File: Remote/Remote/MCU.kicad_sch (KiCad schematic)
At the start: 21 parts, among them J3 61300511121, J4 M20-9990246, U3 STM32G030F6Px, U4 NRF24L01_Breakout

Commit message: Added footprints
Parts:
- C5: footprint (none) -> Power_:CAPC1608X90N
- C6: footprint (none) -> MCU_:CAPC1005X55N
- R4: footprint (none) -> MCU_:RESC2012X65N
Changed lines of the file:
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@@
       (effects (font (size 1.27 1.27)))
     )
-    (property "Footprint" "" (at 148.59 120.9548 0)
+    (property "Footprint" "Power_:CAPC1608X90N" (at 148.59 120.9548 0)
       (effects (font (size 1.27 1.27)) hide)
     )
@@
       (effects (font (size 1.27 1.27)))
     )
-    (property "Footprint" "" (at 148.59 126.0348 0)
-      (effects (font (size 1.27 1.27)) hide)
-    )
-    (property "Datasheet" "~" (at 144.78 127 0)
+    (property "Footprint" "MCU_:CAPC1005X55N" (at 148.59 126.0348 0)
+      (effects (font (size 1.27 1.27)) hide)
+    )
+    (property "Datasheet" "CL05A104KA5NNNC" (at 144.78 127 0)
       (effects (font (size 1.27 1.27)) hide)
     )
@@
       (effects (font (size 1.27 1.27)))
     )
-    (property "Footprint" "" (at 207.01 103.378 90)
-      (effects (font (size 1.27 1.27)) hide)
-    )
-    (property "Datasheet" "~" (at 207.01 101.6 0)
-      (effects (font (size 1.27 1.27)) hide)
-    )
+    (property "Footprint" "MCU_:RESC2012X65N" (at 207.01 103.378 90)
+      (effects (font (size 1.27 1.27)) hide)
+    )
+    (property "Datasheet" "ESR10EZPF1200" (at 207.01 101.6 0)
+      (effects (font (size 1.27 1.27)) hide)
+    )

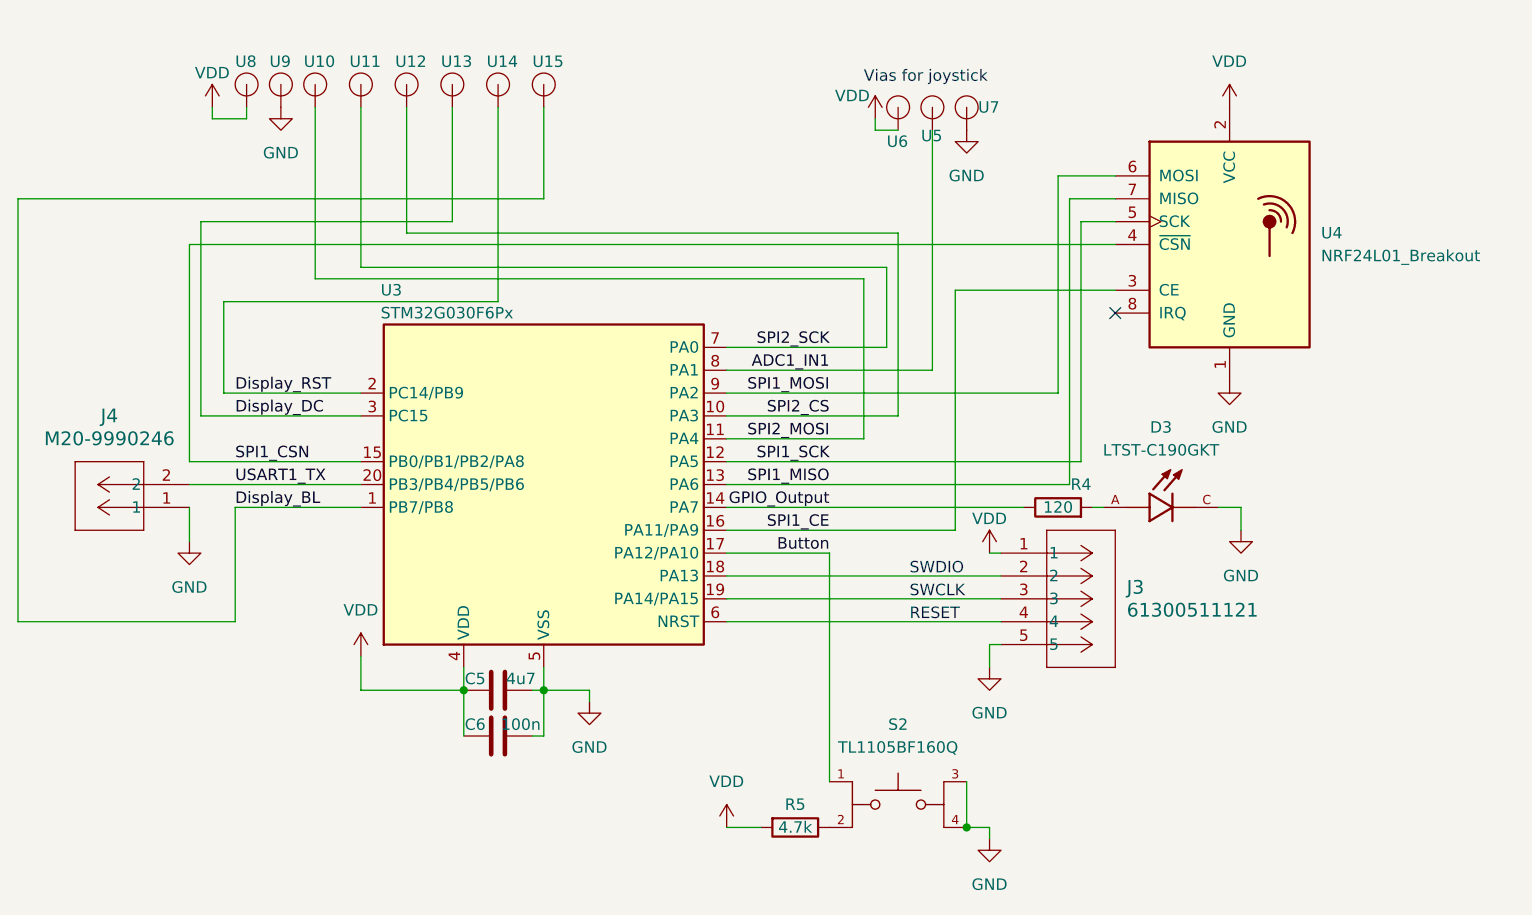
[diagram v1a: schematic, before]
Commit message: Finished with remote V1 PCB
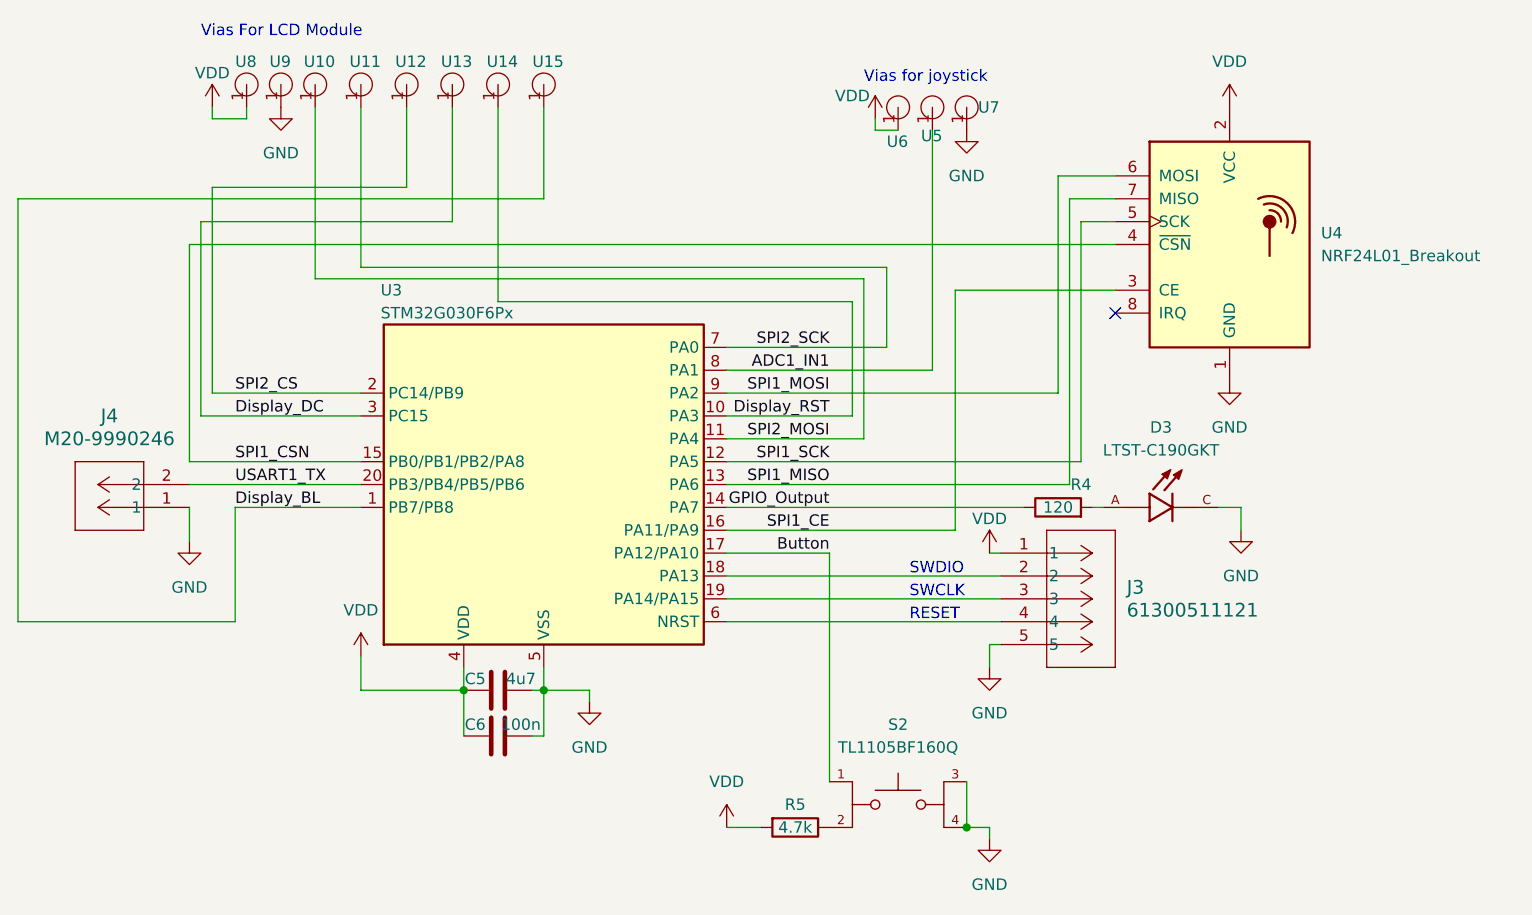
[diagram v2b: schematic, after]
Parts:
- R5: footprint (none) -> Power_:RESC1005X40N
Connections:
- net ADC1_IN1: now also U5.1; no longer U5.
- net Display_BL: now also U15.1; no longer U15.
- net Display_DC: now also U13.1; no longer U13.
- net Display_RST: now also U14.1, U3.10 (PA3); no longer U14., U3.2 (PC14/PB9)
- net GND: now also U7.1, U9.1; no longer U7., U9.
- net SPI2_CS: now also U12.1, U3.2 (PC14/PB9); no longer U12., U3.10 (PA3)
- net SPI2_MOSI: now also U10.1; no longer U10.
- net SPI2_SCK: now also U11.1; no longer U11.
- net VDD: now also U6.1, U8.1; no longer U6., U8.
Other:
- note added: "Vias For LCD Module"
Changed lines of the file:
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@@
     (stroke (width 0) (type default))
   )
-  (wire (pts (xy 189.23 71.12) (xy 189.23 91.44))
+  (wire (pts (xy 134.62 66.04) (xy 113.03 66.04))
     (stroke (width 0) (type default))
   )
@@
     (stroke (width 0) (type default))
   )
+  (wire (pts (xy 113.03 88.9) (xy 129.54 88.9))
+    (stroke (width 0) (type default))
+  )
   (wire (pts (xy 209.55 69.85) (xy 209.55 96.52))
     (stroke (width 0) (type default))
@@
     (stroke (width 0) (type default))
   )
-  (wire (pts (xy 114.3 88.9) (xy 129.54 88.9))
-    (stroke (width 0) (type default))
-  )
   (wire (pts (xy 110.49 72.39) (xy 110.49 96.52))
     (stroke (width 0) (type default))
@@
     (stroke (width 0) (type default))
   )
-  (wire (pts (xy 114.3 78.74) (xy 114.3 88.9))
-    (stroke (width 0) (type default))
-  )
   (wire (pts (xy 111.76 91.44) (xy 129.54 91.44))
     (stroke (width 0) (type default))
@@
     (stroke (width 0) (type default))
   )
-  (wire (pts (xy 134.62 57.15) (xy 134.62 71.12))
-    (stroke (width 0) (type default))
-  )
   (wire (pts (xy 129.54 74.93) (xy 187.96 74.93))
     (stroke (width 0) (type default))
@@
     (stroke (width 0) (type default))
   )
+  (wire (pts (xy 184.15 78.74) (xy 184.15 91.44))
+    (stroke (width 0) (type default))
+  )
   (wire (pts (xy 91.44 114.3) (xy 115.57 114.3))
     (stroke (width 0) (type default))
   )
-  (wire (pts (xy 134.62 71.12) (xy 189.23 71.12))
+  (wire (pts (xy 134.62 57.15) (xy 134.62 66.04))
     (stroke (width 0) (type default))
   )
@@
     (stroke (width 0) (type default))
   )
+  (wire (pts (xy 144.78 78.74) (xy 184.15 78.74))
+    (stroke (width 0) (type default))
+  )
   (wire (pts (xy 208.28 67.31) (xy 208.28 99.06))
     (stroke (width 0) (type default))
@@
     (stroke (width 0) (type default))
   )
-  (wire (pts (xy 170.18 91.44) (xy 189.23 91.44))
-    (stroke (width 0) (type default))
-  )
   (wire (pts (xy 149.86 119.38) (xy 149.86 121.92))
     (stroke (width 0) (type default))
@@
     (stroke (width 0) (type default))
   )
+  (wire (pts (xy 113.03 66.04) (xy 113.03 88.9))
+    (stroke (width 0) (type default))
+  )
   (wire (pts (xy 187.96 74.93) (xy 187.96 83.82))
     (stroke (width 0) (type default))
@@
     (stroke (width 0) (type default))
   )
+  (wire (pts (xy 170.18 91.44) (xy 184.15 91.44))
+    (stroke (width 0) (type default))
+  )
   (wire (pts (xy 199.39 137.16) (xy 199.39 138.43))
     (stroke (width 0) (type default))
@@
   )
   (wire (pts (xy 213.36 67.31) (xy 208.28 67.31))
-    (stroke (width 0) (type default))
-  )
-  (wire (pts (xy 144.78 78.74) (xy 114.3 78.74))
     (stroke (width 0) (type default))
   )
@@
   )
   (text "Vias for joystick" (at 185.42 54.61 0)
-    (effects (font (size 1.27 1.27)) (justify left bottom))
+    (effects (font (size 1.27 1.27)) (justify left bottom) (href "https://www.adafruit.com/product/444"))
   )
   (text "SWCLK" (at 190.5 111.76 0)
     (effects (font (size 1.27 1.27)) (justify left bottom))
   )
+  (text "Vias For LCD Module" (at 111.76 49.53 0)
+    (effects (font (size 1.27 1.27)) (justify left bottom) (href "https://www.waveshare.com/1.28inch-lcd-module.htm"))
+  )
   (label "GPIO_Output" (at 181.61 101.6 180) (fields_autoplaced)
     (effects (font (size 1.27 1.27)) (justify right bottom))
@@
     (effects (font (size 1.27 1.27)) (justify left bottom))
   )
-  (label "SPI2_CS" (at 181.61 91.44 180) (fields_autoplaced)
-    (effects (font (size 1.27 1.27)) (justify right bottom))
+  (label "SPI2_CS" (at 115.57 88.9 0) (fields_autoplaced)
+    (effects (font (size 1.27 1.27)) (justify left bottom))
   )
   (label "ADC1_IN1" (at 181.61 86.36 180) (fields_autoplaced)
     (effects (font (size 1.27 1.27)) (justify right bottom))
   )
-  (label "Display_RST" (at 115.57 88.9 0) (fields_autoplaced)
-    (effects (font (size 1.27 1.27)) (justify left bottom))
+  (label "Display_RST" (at 181.61 91.44 180) (fields_autoplaced)
+    (effects (font (size 1.27 1.27)) (justify right bottom))
   )
   (label "SPI1_MOSI" (at 181.61 88.9 180) (fields_autoplaced)
@@
       (effects (font (size 1.27 1.27)) hide)
     )
-    (pin "")
+    (pin "1")
     (instances
       (project "Remote"
@@
       (effects (font (size 1.27 1.27)) hide)
     )
-    (pin "")
+    (pin "1")
     (instances
       (project "Remote"
@@
       (effects (font (size 1.27 1.27)) hide)
     )
-    (pin "")
+    (pin "1")
     (instances
       (project "Remote"
@@
       (effects (font (size 1.27 1.27)) hide)
     )
-    (pin "")
+    (pin "1")
     (instances
       (project "Remote"
@@
       (effects (font (size 1.27 1.27)) hide)
     )
-    (pin "")
+    (pin "1")
     (instances
       (project "Remote"
@@
       (effects (font (size 1.27 1.27)))
     )
-    (property "Footprint" "" (at 177.8 135.382 90)
-      (effects (font (size 1.27 1.27)) hide)
-    )
-    (property "Datasheet" "~" (at 177.8 137.16 0)
+    (property "Footprint" "Power_:RESC1005X40N" (at 177.8 135.382 90)
+      (effects (font (size 1.27 1.27)) hide)
+    )
+    (property "Datasheet" "RC0402FR-074K7L" (at 177.8 137.16 0)
       (effects (font (size 1.27 1.27)) hide)
     )
@@
       (effects (font (size 1.27 1.27)) hide)
     )
-    (pin "")
+    (pin "1")
     (instances
       (project "Remote"
@@
       (effects (font (size 1.27 1.27)) hide)
     )
-    (pin "")
+    (pin "1")
     (instances
       (project "Remote"
@@
       (effects (font (size 1.27 1.27)) hide)
     )
-    (pin "")
+    (pin "1")
     (instances
       (project "Remote"
@@
       (effects (font (size 1.27 1.27)) hide)
     )
-    (pin "")
+    (pin "1")
     (instances
       (project "Remote"
@@
       (effects (font (size 1.27 1.27)) hide)
     )
-    (pin "")
+    (pin "1")
     (instances
       (project "Remote"
@@
       (effects (font (size 1.27 1.27)) hide)
     )
-    (pin "")
-    (instances
-      (project "Remote"
+    (pin "1")
+    (instances
+      (project "Remote"
